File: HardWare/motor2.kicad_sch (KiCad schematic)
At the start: 48 parts, among them J4 hall, J5 Conn_01x03, Q10 Q_NMOS_SGD, Q11 Q_NMOS_SGD, Q12 Q_NMOS_SGD, Q7 Q_NMOS_SGD, Q8 Q_NMOS_SGD, Q9 Q_NMOS_SGD, U5 DRV8301DCAR

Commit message: Add PCB
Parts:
- J4: footprint Connector_Molex:Molex_CLIK-Mate_502382-0570_1x05-1MP_P1.25mm_Vertical -> Connector_Molex:Molex_CLIK-Mate_502386-0570_1x05-1MP_P1.25mm_Horizontal
- J5: footprint Connector:Banana_Jack_3Pin -> USER:MR30-M
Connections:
- net M1_GH_A is gone; now on net M2_GH_A: U5.47 (GH_A)
- net M1_GH_B is gone; now on net M2_GH_B: U5.42 (GH_B)
- net M1_GH_C is gone; now on net M2_GH_C: U5.37 (GH_C)
- net M1_GL_A is gone; now on net M2_GL_A: U5.45 (GL_A)
- net M1_GL_B is gone; now on net M2_GL_B: U5.40 (GL_B)
- net M1_GL_C is gone; now on net M2_GL_C: U5.35 (GL_C)
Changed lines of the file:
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@@
     (effects (font (size 1.27 1.27)) (justify right bottom))
   )
-  (label "M1_GL_A" (at 88.9 102.87 0)
+  (label "M2_GL_A" (at 88.9 102.87 0)
     (effects (font (size 1.27 1.27)) (justify left bottom))
   )
@@
     (effects (font (size 1.27 1.27)) (justify right bottom))
   )
-  (label "M1_GH_B" (at 88.9 97.79 0)
+  (label "M2_GH_B" (at 88.9 97.79 0)
     (effects (font (size 1.27 1.27)) (justify left bottom))
   )
@@
     (effects (font (size 1.27 1.27)) (justify left bottom))
   )
-  (label "M1_GH_A" (at 88.9 95.25 0)
+  (label "M2_GH_A" (at 88.9 95.25 0)
     (effects (font (size 1.27 1.27)) (justify left bottom))
   )
@@
     (effects (font (size 1.27 1.27)) (justify right bottom))
   )
-  (label "M1_GL_B" (at 88.9 105.41 0)
+  (label "M2_GL_B" (at 88.9 105.41 0)
     (effects (font (size 1.27 1.27)) (justify left bottom))
   )
@@
     (effects (font (size 1.27 1.27)) (justify right bottom))
   )
-  (label "M1_GL_C" (at 88.9 107.95 0)
+  (label "M2_GL_C" (at 88.9 107.95 0)
     (effects (font (size 1.27 1.27)) (justify left bottom))
   )
@@
     (effects (font (size 1.27 1.27)) (justify right bottom))
   )
-  (label "M1_GH_C" (at 88.9 100.33 0)
+  (label "M2_GH_C" (at 88.9 100.33 0)
     (effects (font (size 1.27 1.27)) (justify left bottom))
   )
@@
       (effects (font (size 1.27 1.27)) (justify left))
     )
-    (property "Footprint" "Connector_Molex:Molex_CLIK-Mate_502382-0570_1x05-1MP_P1.25mm_Vertical" (id 2) (at 265.43 41.91 0)
+    (property "Footprint" "Connector_Molex:Molex_CLIK-Mate_502386-0570_1x05-1MP_P1.25mm_Horizontal" (id 2) (at 265.43 41.91 0)
       (effects (font (size 1.27 1.27)) hide)
     )
@@
       (effects (font (size 1.27 1.27)) (justify left))
     )
-    (property "Footprint" "Connector:Banana_Jack_3Pin" (id 2) (at 270.51 127 0)
-      (effects (font (size 1.27 1.27)) hide)
-    )
+    (property "Footprint" "USER:MR30-M" (id 2) (at 270.51 127 0)
+      (effects (font (size 1.27 1.27)) hide)
+    )

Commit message: 增加一些功率器件有关的pcb电路
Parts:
- removed R38: 0.0005, Resistor_SMD:R_2512_6332Metric, symbol Device:R
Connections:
- net M2_SL_A is gone; now on net GND1: Q8.1 (S), U5.44 (SL_A)
- net A: now reaches J5.1 (Pin_1), Q7.1 (S), Q8.3 (D)
- net B: now reaches J5.2 (Pin_2), Q10.3 (D), Q9.1 (S)
- net C: now reaches J5.3 (Pin_3), Q11.1 (S), Q12.3 (D)
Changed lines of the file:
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@@
-    (stroke (width 0) (type default) (color 0 0 0 0))
-  )
-  (wire (pts (xy 168.91 149.86) (xy 168.91 151.13))
     (stroke (width 0) (type default) (color 0 0 0 0))
   )
@@
     (stroke (width 0) (type default) (color 0 0 0 0))
   )
-  (wire (pts (xy 168.91 142.24) (xy 168.91 140.97))
+  (wire (pts (xy 168.91 140.97) (xy 168.91 151.13))
     (stroke (width 0) (type default) (color 0 0 0 0))
   )
@@
     (effects (font (size 1.27 1.27)) (justify right bottom))
   )
+  (label "B" (at 256.54 127 0)
+    (effects (font (size 1.27 1.27)) (justify left bottom))
+  )
   (label "M2_GH_C" (at 88.9 100.33 0)
+    (effects (font (size 1.27 1.27)) (justify left bottom))
+  )
+  (label "A" (at 256.54 124.46 0)
+    (effects (font (size 1.27 1.27)) (justify left bottom))
+  )
+  (label "C" (at 256.54 129.54 0)
     (effects (font (size 1.27 1.27)) (justify left bottom))
   )
@@
     (pin "1")
   )
-  (symbol (lib_id "Device:R") (at 168.91 146.05 0) (unit 1)
-    (in_bom yes) (on_board yes) (fields_autoplaced)
-    (property "Reference" "R38" (id 0) (at 171.45 144.7799 0)
-      (effects (font (size 1.27 1.27)) (justify left))
-    )
-    (property "Value" "0.0005" (id 1) (at 171.45 147.3199 0)
-      (effects (font (size 1.27 1.27)) (justify left))
-    )
-    (property "Footprint" "Resistor_SMD:R_2512_6332Metric" (id 2) (at 167.132 146.05 90)
-      (effects (font (size 1.27 1.27)) hide)
-    )
-    (property "Datasheet" "~" (id 3) (at 168.91 146.05 0)
-      (effects (font (size 1.27 1.27)) hide)
-    )
-    (pin "1")
-    (pin "2")
-  )
   (symbol (lib_id "Device:R") (at 193.04 118.11 90) (unit 1)

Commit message: 修改一些BUG
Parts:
- J4: footprint Connector_Molex:Molex_CLIK-Mate_502386-0570_1x05-1MP_P1.25mm_Horizontal -> USER:M1010RS-05P
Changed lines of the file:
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@@
       (effects (font (size 1.27 1.27)) (justify left))
     )
-    (property "Footprint" "Connector_Molex:Molex_CLIK-Mate_502386-0570_1x05-1MP_P1.25mm_Horizontal" (id 2) (at 265.43 41.91 0)
+    (property "Footprint" "USER:M1010RS-05P" (id 2) (at 265.43 41.91 0)
       (effects (font (size 1.27 1.27)) hide)
     )

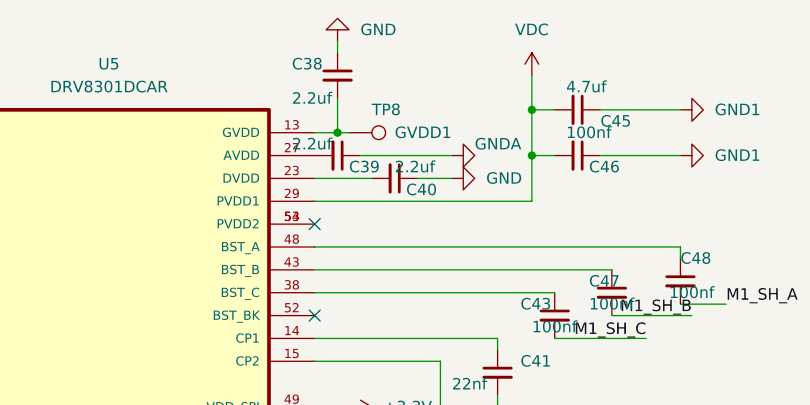
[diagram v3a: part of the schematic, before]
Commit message: 更新一些信号电源
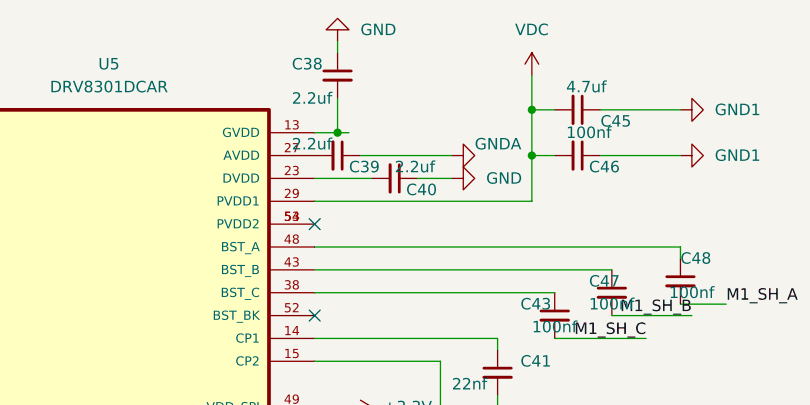
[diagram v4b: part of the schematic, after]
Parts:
- removed TP8: GVDD1, TestPoint:TestPoint_THTPad_D2.0mm_Drill1.0mm, symbol Connector:TestPoint
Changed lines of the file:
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@@
     (pin "2")
   )
-  (symbol (lib_id "Connector:TestPoint") (at 92.71 34.29 270) (unit 1)
-    (in_bom yes) (on_board yes)
-    (property "Reference" "TP8" (id 0) (at 95.25 31.75 90)
-      (effects (font (size 1.27 1.27)) (justify left))
-    )
-    (property "Value" "GVDD1" (id 1) (at 97.79 34.29 90)
-      (effects (font (size 1.27 1.27)) (justify left))
-    )
-    (property "Footprint" "TestPoint:TestPoint_THTPad_D2.0mm_Drill1.0mm" (id 2) (at 92.71 39.37 0)
-      (effects (font (size 1.27 1.27)) hide)
-    )
-    (property "Datasheet" "~" (id 3) (at 92.71 39.37 0)
-      (effects (font (size 1.27 1.27)) hide)
-    )
-    (pin "1")
-  )
 )

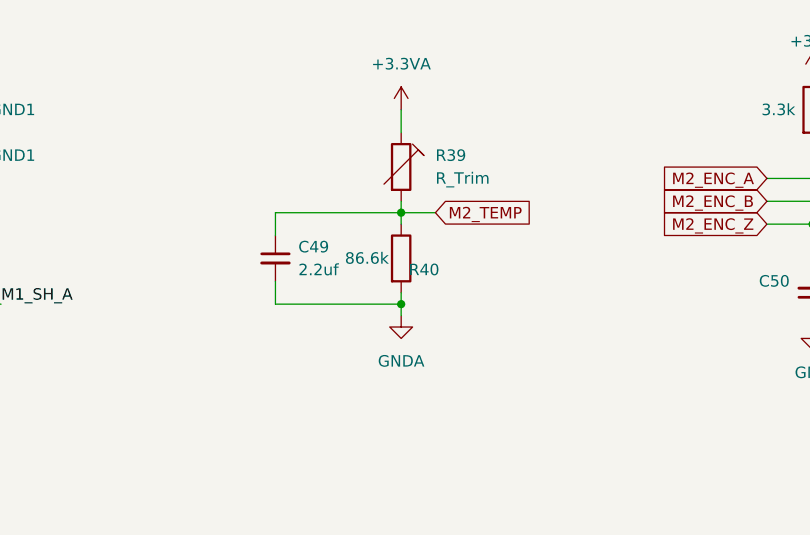
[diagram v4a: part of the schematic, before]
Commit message: 修改pcb中信号部分
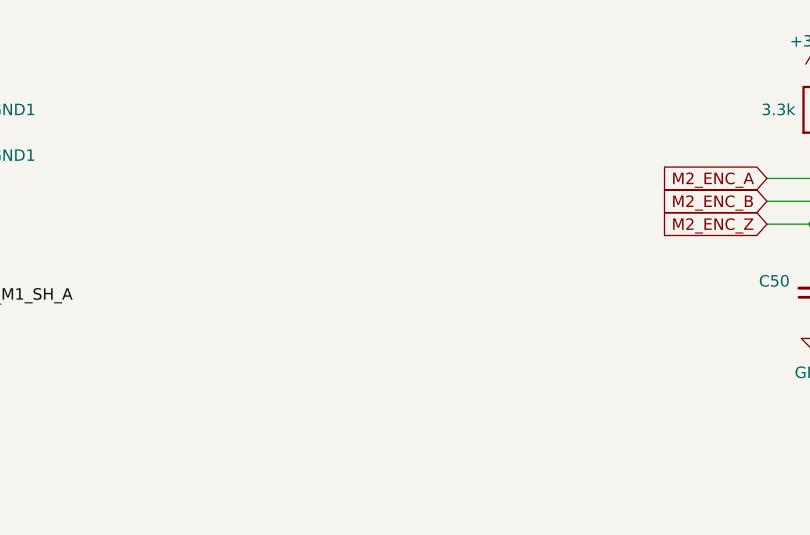
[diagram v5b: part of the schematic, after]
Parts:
- removed C49: 2.2uf, Capacitor_SMD:C_0603_1608Metric, symbol Device:C_Small
- removed R39: R_Trim, Resistor_SMD:R_0603_1608Metric, symbol Device:R_Trim
- removed R40: 86.6k, Resistor_SMD:R_0603_1608Metric, symbol Device:R
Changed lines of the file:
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@@
   (junction (at 205.74 139.7) (diameter 0) (color 0 0 0 0)
   )
-  (junction (at 179.07 53.34) (diameter 0) (color 0 0 0 0)
-  )
   (junction (at 33.02 148.59) (diameter 0) (color 0 0 0 0)
-  )
-  (junction (at 179.07 43.18) (diameter 0) (color 0 0 0 0)
   )
   (junction (at 205.74 127) (diameter 0) (color 0 0 0 0)
@@
     (stroke (width 0) (type default) (color 0 0 0 0))
   )
-  (wire (pts (xy 179.07 43.18) (xy 179.07 44.45))
-    (stroke (width 0) (type default) (color 0 0 0 0))
-  )
   (wire (pts (xy 257.81 36.83) (xy 257.81 35.56))
     (stroke (width 0) (type default) (color 0 0 0 0))
@@
     (stroke (width 0) (type default) (color 0 0 0 0))
   )
-  (wire (pts (xy 165.1 45.72) (xy 165.1 43.18))
-    (stroke (width 0) (type default) (color 0 0 0 0))
-  )
   (wire (pts (xy 88.9 46.99) (xy 129.54 46.99))
     (stroke (width 0) (type default) (color 0 0 0 0))
@@
     (stroke (width 0) (type default) (color 0 0 0 0))
   )
-  (wire (pts (xy 179.07 53.34) (xy 179.07 54.61))
-    (stroke (width 0) (type default) (color 0 0 0 0))
-  )
   (wire (pts (xy 33.02 162.56) (xy 41.91 162.56))
     (stroke (width 0) (type default) (color 0 0 0 0))
@@
     (stroke (width 0) (type default) (color 0 0 0 0))
   )
-  (wire (pts (xy 165.1 53.34) (xy 179.07 53.34))
-    (stroke (width 0) (type default) (color 0 0 0 0))
-  )
   (wire (pts (xy 233.68 149.86) (xy 242.57 149.86))
     (stroke (width 0) (type default) (color 0 0 0 0))
@@
     (stroke (width 0) (type default) (color 0 0 0 0))
   )
-  (wire (pts (xy 179.07 41.91) (xy 179.07 43.18))
-    (stroke (width 0) (type default) (color 0 0 0 0))
-  )
   (wire (pts (xy 236.22 41.91) (xy 236.22 49.53))
     (stroke (width 0) (type default) (color 0 0 0 0))
@@
     (stroke (width 0) (type default) (color 0 0 0 0))
   )
-  (wire (pts (xy 165.1 43.18) (xy 179.07 43.18))
-    (stroke (width 0) (type default) (color 0 0 0 0))
-  )
   (wire (pts (xy 242.57 109.22) (xy 242.57 113.03))
     (stroke (width 0) (type default) (color 0 0 0 0))
@@
     (stroke (width 0) (type default) (color 0 0 0 0))
   )
-  (wire (pts (xy 179.07 52.07) (xy 179.07 53.34))
-    (stroke (width 0) (type default) (color 0 0 0 0))
-  )
   (wire (pts (xy 92.71 34.29) (xy 91.44 34.29))
     (stroke (width 0) (type default) (color 0 0 0 0))
@@
     (stroke (width 0) (type default) (color 0 0 0 0))
   )
-  (wire (pts (xy 179.07 31.75) (xy 179.07 34.29))
-    (stroke (width 0) (type default) (color 0 0 0 0))
-  )
   (wire (pts (xy 109.22 113.03) (xy 121.92 113.03))
     (stroke (width 0) (type default) (color 0 0 0 0))
@@
   )
   (wire (pts (xy 93.98 36.83) (xy 104.14 36.83))
-    (stroke (width 0) (type default) (color 0 0 0 0))
-  )
-  (wire (pts (xy 179.07 43.18) (xy 182.88 43.18))
-    (stroke (width 0) (type default) (color 0 0 0 0))
-  )
-  (wire (pts (xy 165.1 50.8) (xy 165.1 53.34))
     (stroke (width 0) (type default) (color 0 0 0 0))
   )
@@
     )
   )
-  (global_label "M2_TEMP" (shape input) (at 182.88 43.18 0) (fields_autoplaced)
-    (effects (font (size 1.27 1.27)) (justify left))
-    (property "Intersheet References" "${INTERSHEET_REFS}" (id 0) (at 193.7598 43.1006 0)
-      (effects (font (size 1.27 1.27)) (justify left) hide)
-    )
-  )
   (global_label "M2_ENC_Z" (shape input) (at 219.71 44.45 180) (fields_autoplaced)
     (effects (font (size 1.27 1.27)) (justify right))
@@
     )
     (property "Datasheet" "" (id 3) (at 129.54 36.83 0)
-      (effects (font (size 1.27 1.27)) hide)
-    )
-    (pin "1")
-  )
-  (symbol (lib_id "power:+3.3VA") (at 179.07 31.75 0) (unit 1)
-    (in_bom yes) (on_board yes) (fields_autoplaced)
-    (property "Reference" "#PWR085" (id 0) (at 179.07 35.56 0)
-      (effects (font (size 1.27 1.27)) hide)
-    )
-    (property "Value" "+3.3VA" (id 1) (at 179.07 26.67 0))
-    (property "Footprint" "" (id 2) (at 179.07 31.75 0)
-      (effects (font (size 1.27 1.27)) hide)
-    )
-    (property "Datasheet" "" (id 3) (at 179.07 31.75 0)
       (effects (font (size 1.27 1.27)) hide)
     )
@@
     (pin "2")
   )
-  (symbol (lib_id "power:GNDA") (at 179.07 54.61 0) (unit 1)
-    (in_bom yes) (on_board yes) (fields_autoplaced)
-    (property "Reference" "#PWR086" (id 0) (at 179.07 60.96 0)
-      (effects (font (size 1.27 1.27)) hide)
-    )
-    (property "Value" "GNDA" (id 1) (at 179.07 59.69 0))
-    (property "Footprint" "" (id 2) (at 179.07 54.61 0)
-      (effects (font (size 1.27 1.27)) hide)
-    )
-    (property "Datasheet" "" (id 3) (at 179.07 54.61 0)
-      (effects (font (size 1.27 1.27)) hide)
-    )
-    (pin "1")
-  )
   (symbol (lib_id "Connector_Generic_MountingPin:Conn_01x05_MountingPin") (at 265.43 41.91 0) (unit 1)
     (in_bom yes) (on_board yes) (fields_autoplaced)
@@
     (pin "3")
   )
-  (symbol (lib_id "Device:R") (at 179.07 48.26 0) (unit 1)
-    (in_bom yes) (on_board yes)
-    (property "Reference" "R40" (id 0) (at 181.61 49.53 0))
-    (property "Value" "86.6k" (id 1) (at 175.26 48.26 0))
-    (property "Footprint" "Resistor_SMD:R_0603_1608Metric" (id 2) (at 177.292 48.26 90)
-      (effects (font (size 1.27 1.27)) hide)
-    )
-    (property "Datasheet" "~" (id 3) (at 179.07 48.26 0)
-      (effects (font (size 1.27 1.27)) hide)
-    )
-    (pin "1")
-    (pin "2")
-  )
   (symbol (lib_id "Device:R") (at 45.72 162.56 90) (unit 1)
     (in_bom yes) (on_board yes)
@@
     (pin "2")
   )
-  (symbol (lib_id "Device:R_Trim") (at 179.07 38.1 0) (unit 1)
-    (in_bom yes) (on_board yes) (fields_autoplaced)
-    (property "Reference" "R39" (id 0) (at 182.88 36.8299 0)
-      (effects (font (size 1.27 1.27)) (justify left))
-    )
-    (property "Value" "R_Trim" (id 1) (at 182.88 39.3699 0)
-      (effects (font (size 1.27 1.27)) (justify left))
-    )
-    (property "Footprint" "Resistor_SMD:R_0603_1608Metric" (id 2) (at 177.292 38.1 90)
-      (effects (font (size 1.27 1.27)) hide)
-    )
-    (property "Datasheet" "~" (id 3) (at 179.07 38.1 0)
-      (effects (font (size 1.27 1.27)) hide)
-    )
-    (pin "1")
-    (pin "2")
-  )
   (symbol (lib_id "Device:R") (at 45.72 148.59 90) (unit 1)
     (in_bom yes) (on_board yes)
@@
       (effects (font (size 1.27 1.27)) hide)
     )
-    (pin "1")
-    (pin "2")
-  )
-  (symbol (lib_id "Device:C_Small") (at 165.1 48.26 0) (unit 1)
-    (in_bom yes) (on_board yes) (fields_autoplaced)
-    (property "Reference" "C49" (id 0) (at 167.64 46.9962 0)
-      (effects (font (size 1.27 1.27)) (justify left))
-    )
-    (property "Value" "2.2uf" (id 1) (at 167.64 49.5362 0)
-      (effects (font (size 1.27 1.27)) (justify left))
-    )
-    (property "Footprint" "Capacitor_SMD:C_0603_1608Metric" (id 2) (at 165.1 48.26 0)
-      (effects (font (size 1.27 1.27)) hide)
-    )
-    (property "Datasheet" "~" (id 3) (at 165.1 48.26 0)
-      (effects (font (size 1.27 1.27)) hide)
-    )

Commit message: 画一部分的信号
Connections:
- net M1_SH_A is gone; now on net M2_SH_A: C48.2
- net M1_SH_B is gone; now on net M2_SH_B: C47.2
- net M1_SH_C is gone; now on net M2_SH_C: C43.2
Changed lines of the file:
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@@
     (effects (font (size 1.27 1.27)) (justify right bottom))
   )
-  (label "M1_SH_B" (at 130.81 54.61 180)
+  (label "M2_SH_B" (at 130.81 54.61 180)
     (effects (font (size 1.27 1.27)) (justify right bottom))
   )
@@
     (effects (font (size 1.27 1.27)) (justify right bottom))
   )
-  (label "M1_SH_A" (at 134.62 53.34 0)
+  (label "M2_SH_A" (at 134.62 53.34 0)
     (effects (font (size 1.27 1.27)) (justify left bottom))
   )
@@
     (effects (font (size 1.27 1.27)) (justify right bottom))
   )
-  (label "M1_SH_C" (at 125.73 57.15 180)
+  (label "M2_SH_C" (at 125.73 57.15 180)
     (effects (font (size 1.27 1.27)) (justify right bottom))
   )
